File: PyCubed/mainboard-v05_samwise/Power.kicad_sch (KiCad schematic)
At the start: 66 parts, among them J14 Conn_01x06, Q1 IRLML2803, Q2 MBT2222ADW1T1, Q22 NDS8434, Q3 MBT2222ADW1T1, U17 BQ25883RGER, U21 TPS7A4501DCQT, U4 ADM1176-1ARMZ-R7, U5 TPS54226PWPRPWP14_2P31X2P46-L, U6 LT3652HVIMSE#PBF

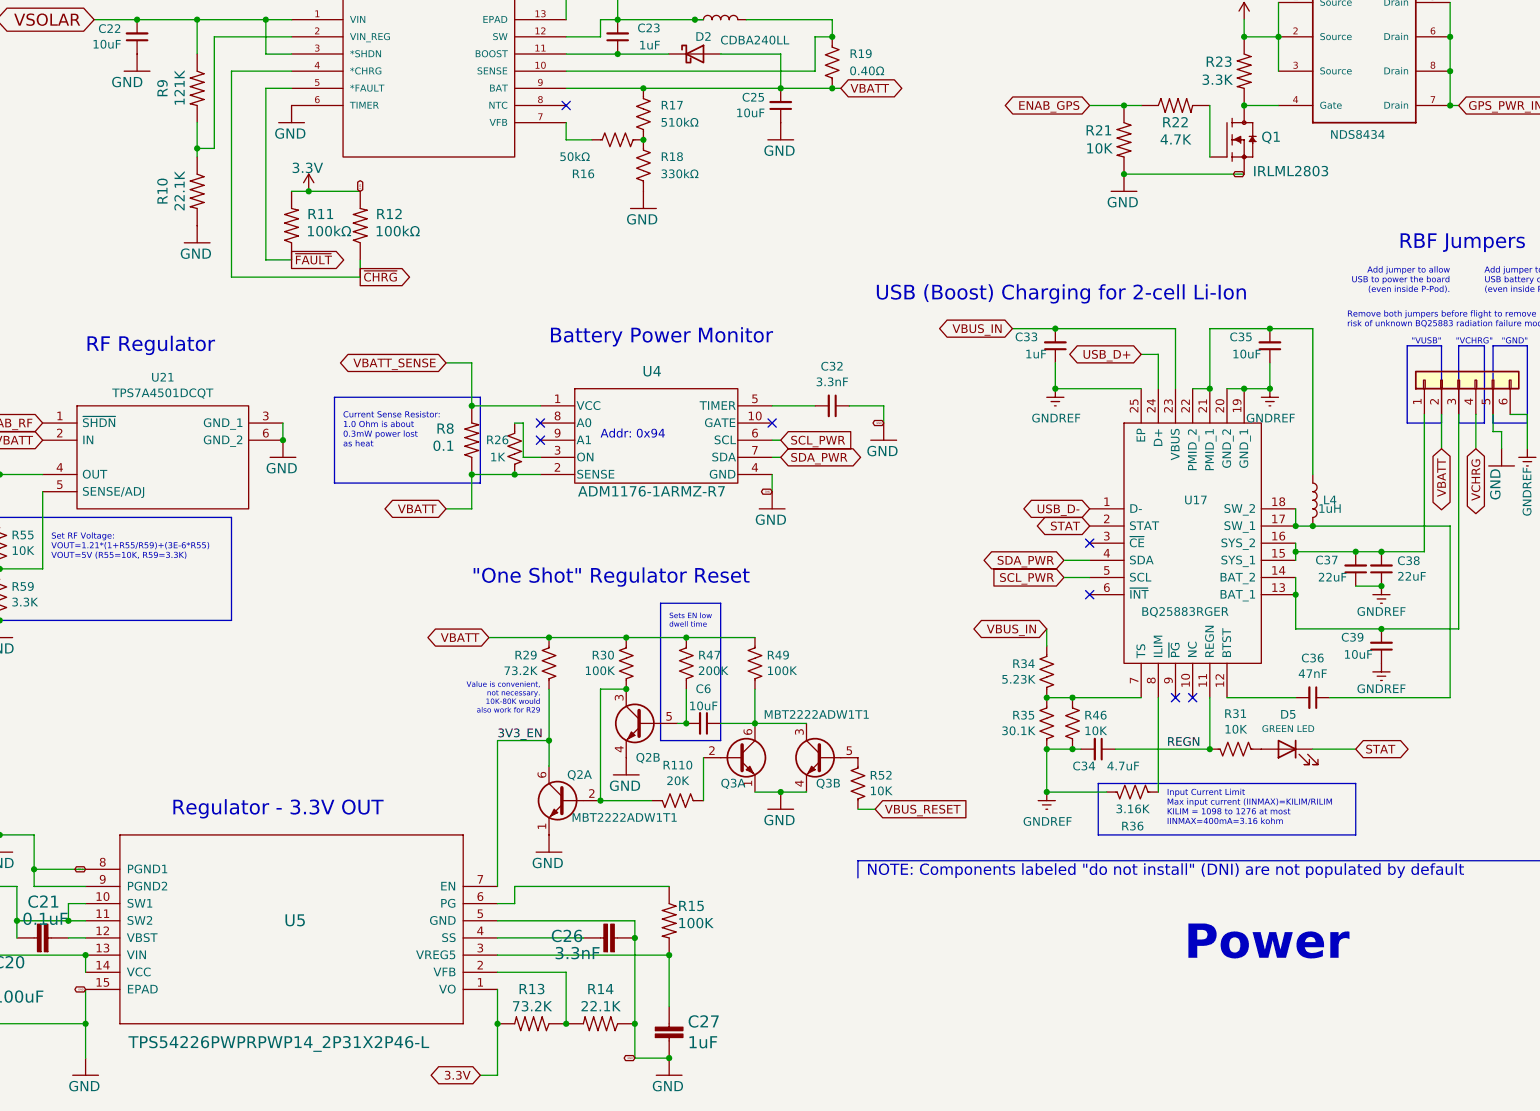
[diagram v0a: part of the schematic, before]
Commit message: added 3D models to Pycubed
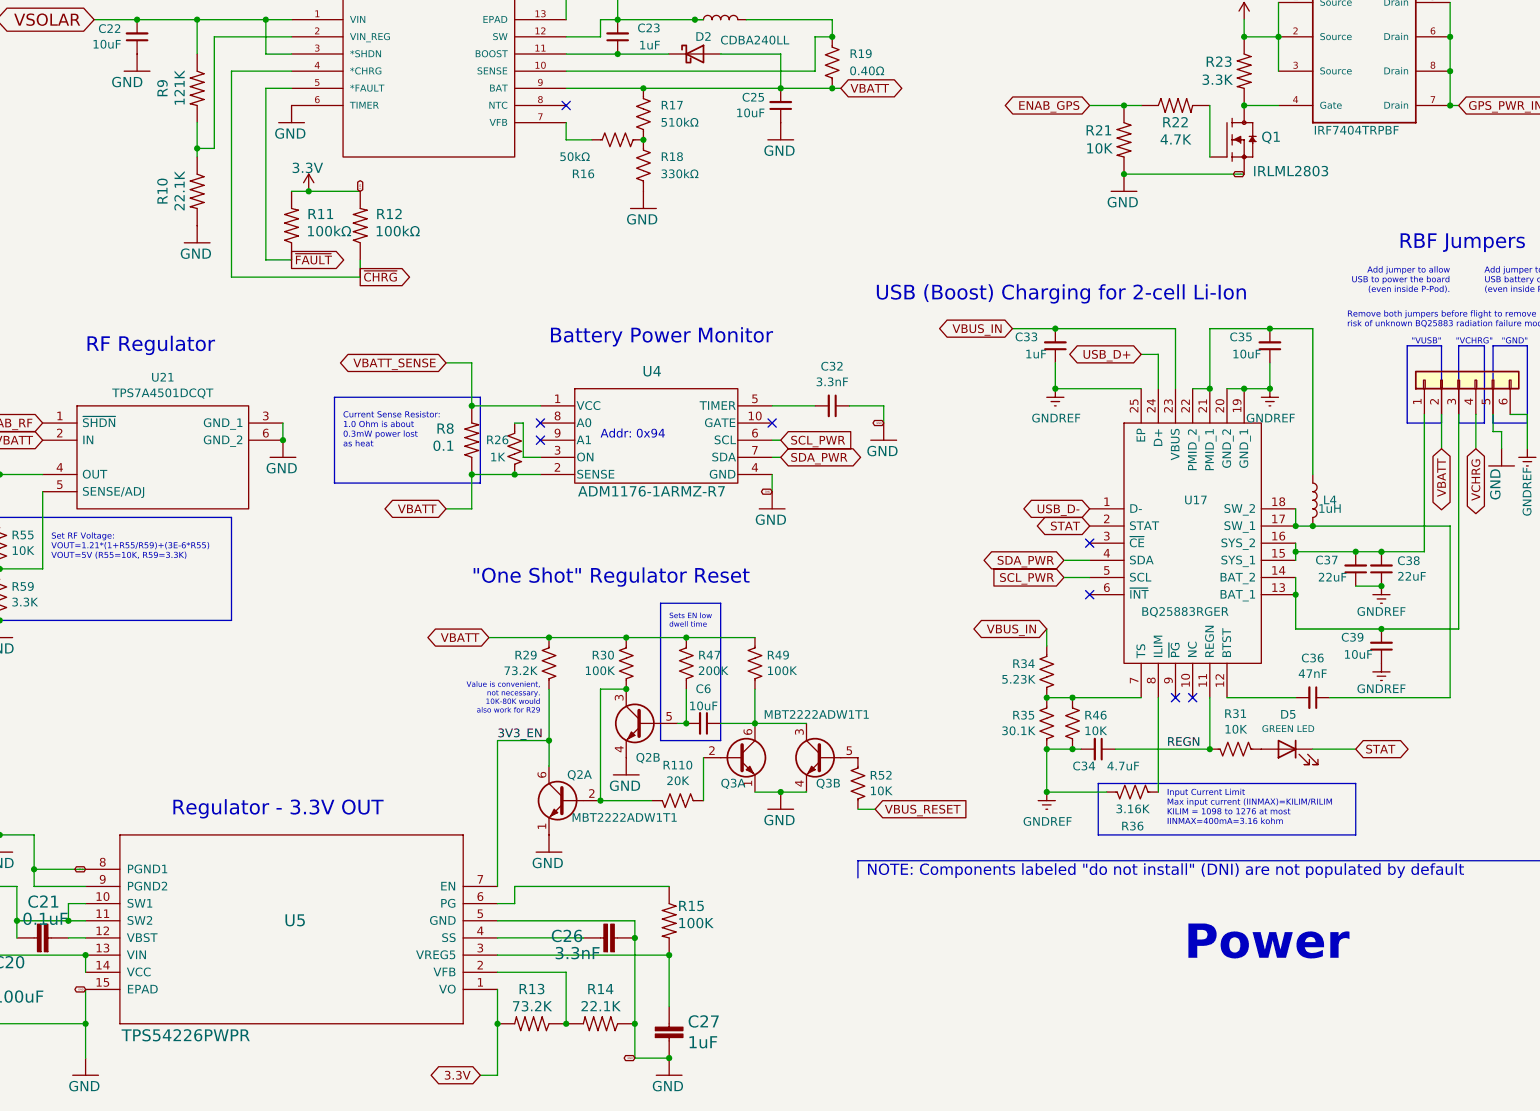
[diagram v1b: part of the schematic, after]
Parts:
- J14: footprint Connector_PinHeader_2.54mm:PinHeader_1x06_P2.54mm_Vertical -> mainboard_local:PinHeader_1x06_P2.54mm_Vertical_J14
- JP6: footprint mainboard:SolderJumper-3_P1.3mm_Bridged12_RoundedPad1.0x1.5mm -> mainboard_local:SolderJumper-3_P1.3mm_Bridged12_RoundedPad1.0x1.5mm_JP6
- Q22: value NDS8434 -> IRF7404TRPBF; footprint mainboard:NDS8434 -> mainboard:IRF7404TRPBF; symbol mainboard:NDS8434 -> mainboard:IRF7404TRPBF; Field7 NDS8434 -> IRF7404TRPBF
- U5: value TPS54226PWPRPWP14_2P31X2P46-L -> TPS54226PWPR
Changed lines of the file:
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@@
     )
   )
-  (symbol (lib_id "mainboard:NDS8434") (at 251.46 43.18 0) (unit 1)
+  (symbol (lib_id "mainboard:IRF7404TRPBF") (at 251.46 43.18 0) (unit 1)
     (in_bom yes) (on_board yes) (dnp no)
     (property "Reference" "Q22" (at 250.19 31.75 0)
       (effects (font (size 1.27 1.27)) (justify left bottom))
     )
-    (property "Value" "NDS8434" (at 246.38 55.88 0)
+    (property "Value" "IRF7404TRPBF" (at 243.967 55.245 0)
       (effects (font (size 1.27 1.27)) (justify left bottom))
     )
-    (property "Footprint" "mainboard:NDS8434" (at 251.46 43.18 0)
+    (property "Footprint" "mainboard:IRF7404TRPBF" (at 251.46 43.18 0)
       (effects (font (size 1.27 1.27)) (justify left bottom) hide)
     )
-    (property "Datasheet" "https://www.onsemi.com/pdf/datasheet/nds8434-d.pdf" (at 251.46 43.18 0)
+    (property "Datasheet" "https://www.infineon.com/dgdl/irf7404pbf.pdf?fileId=5546d462533600a4015355fa31be1ba0" (at 251.46 43.18 0)
       (effects (font (size 1.27 1.27)) (justify left bottom) hide)
     )
@@
       (effects (font (size 1.27 1.27)) (justify left bottom) hide)
     )
-    (property "Field7" "NDS8434" (at 251.46 43.18 0)
+    (property "Field7" "IRF7404TRPBF" (at 251.46 43.18 0)
       (effects (font (size 1.27 1.27)) (justify left bottom) hide)
     )
@@
       (effects (font (size 1.27 1.27)) (justify right) hide)
     )
-    (property "Footprint" "Connector_PinHeader_2.54mm:PinHeader_1x06_P2.54mm_Vertical" (at 265.43 91.44 0)
+    (property "Footprint" "mainboard_local:PinHeader_1x06_P2.54mm_Vertical_J14" (at 265.43 91.44 0)
       (effects (font (size 1.27 1.27)) hide)
     )
@@
       (effects (font (size 1.27 1.27)) (justify left) hide)
     )
-    (property "Footprint" "mainboard:SolderJumper-3_P1.3mm_Bridged12_RoundedPad1.0x1.5mm" (at 30.48 100.33 0)
+    (property "Footprint" "mainboard_local:SolderJumper-3_P1.3mm_Bridged12_RoundedPad1.0x1.5mm_JP6" (at 30.48 100.33 0)
       (effects (font (size 1.27 1.27)) hide)
     )
@@
       (effects (font (size 1.7526 1.7526)) (justify left bottom))
     )
-    (property "Value" "TPS54226PWPRPWP14_2P31X2P46-L" (at 68.58 190.5 0)
+    (property "Value" "TPS54226PWPR" (at 67.564 189.484 0)
       (effects (font (size 1.7526 1.7526)) (justify right top))
     )

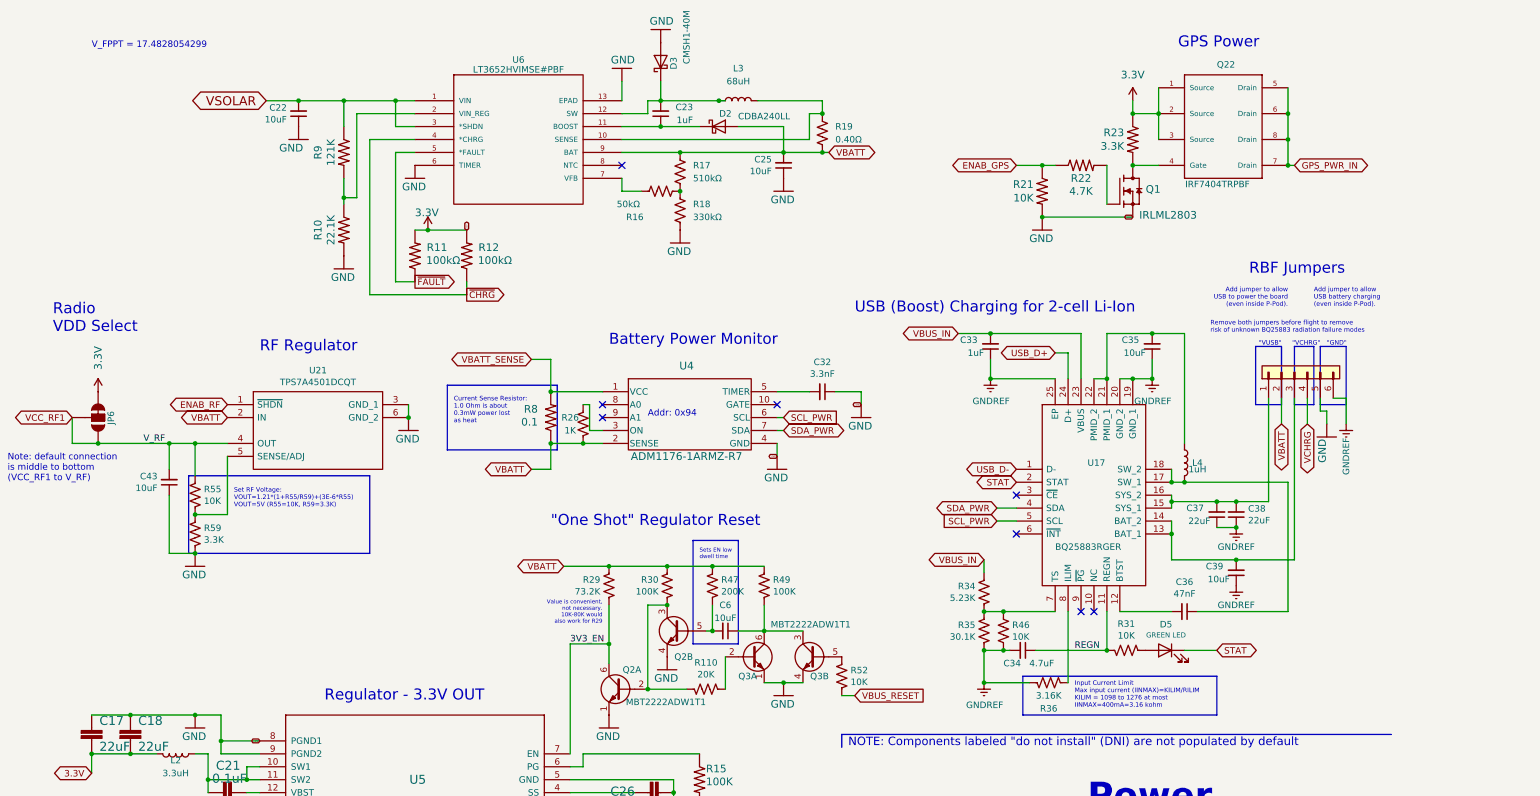
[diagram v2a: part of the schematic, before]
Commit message: Deleted some things, added TODOs to Pycubed
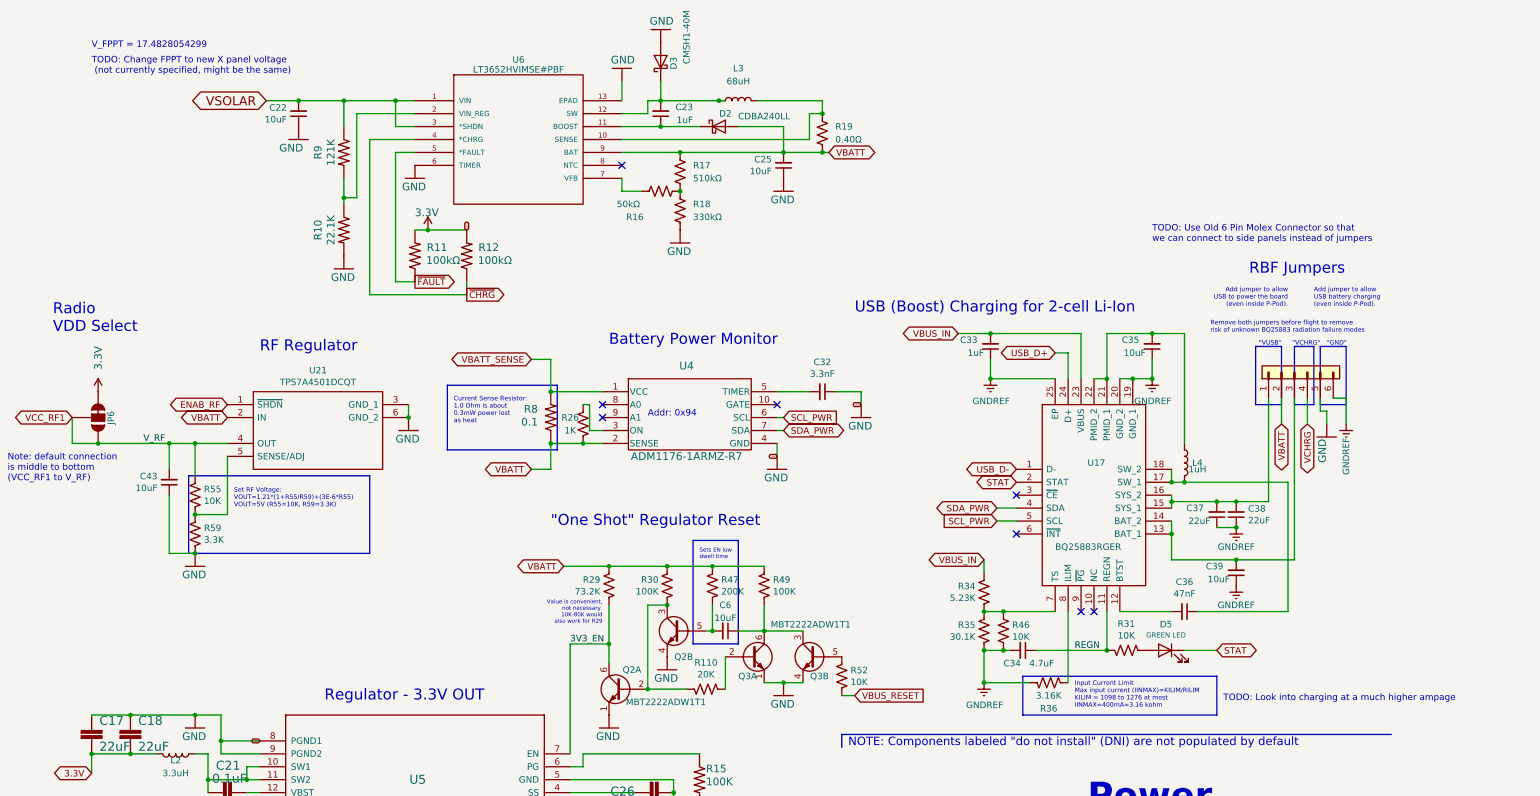
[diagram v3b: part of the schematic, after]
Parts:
- removed Q1: IRLML2803, mainboard:SOT-23, symbol mainboard:IRLML2803TRPBF
- removed Q22: IRF7404TRPBF, mainboard:IRF7404TRPBF, symbol mainboard:IRF7404TRPBF
- removed R21: 10K, Resistor_SMD:R_0603_1608Metric, symbol mainboard:R-US_R0603
- removed R22: 4.7K, Resistor_SMD:R_0603_1608Metric, symbol mainboard:R-US_R0603
- removed R23: 3.3K, Resistor_SMD:R_0603_1608Metric, symbol mainboard:R-US_R0603
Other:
- note added: "TODO: Change FPPT to new X panel voltage (not currently specified, might be the same)"
- note added: "TODO: Look into charging at a much higher ampage"
- note added: "TODO: Use Old 6 Pin Molex Connector so that we can connect to side panels instead of jumpers"
- note removed: "GPS Power"

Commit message: made some changes to mainboard
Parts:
- added J19: Conn_01x06, symbol Connector_Generic:Conn_01x06
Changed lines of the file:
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@@
   )
   (text "Remove both jumpers before flight to remove\nrisk of unknown BQ25883 radiation failure modes\n"
-    (at 248.92 83.82 0)
+    (at 220.98 50.8 0)
     (effects (font (size 0.889 0.889)) (justify left bottom))
   )
@@
   )
   (text "TODO: Use Old 6 Pin Molex Connector so that \nwe can connect to side panels instead of jumpers\n"
-    (at 237.49 66.04 0)
+    (at 353.06 55.88 0)
     (effects (font (size 1.27 1.27) (color 255 0 0 1)) (justify left bottom))
   )
@@
   )
   (text "Add jumper to allow\nUSB to power the board\n(even inside P-Pod).\n"
-    (at 264.16 78.74 0)
+    (at 236.22 45.72 0)
     (effects (font (size 0.889 0.889)) (justify right bottom))
   )
@@
     (effects (font (size 1.651 1.651)) (justify left bottom))
   )
-  (text "RBF Jumpers" (at 256.54 72.39 0)
+  (text "RBF Jumpers" (at 228.6 39.37 0)
     (effects (font (size 2.159 2.159)) (justify left bottom))
   )
   (text "Add jumper to allow\nUSB battery charging\n(even inside P-Pod).\n"
-    (at 269.24 78.74 0)
+    (at 241.3 45.72 0)
     (effects (font (size 0.889 0.889)) (justify left bottom))
   )
@@
         )
       )
+    )
+  )
+  (symbol (lib_id "Connector_Generic:Conn_01x06") (at 264.16 58.42 90) (unit 1)
+    (in_bom yes) (on_board yes) (dnp no) (fields_autoplaced)
+    (property "Reference" "J19" (at 265.43 52.07 90)
+      (effects (font (size 1.27 1.27)))
+    )
+    (property "Value" "Conn_01x06" (at 265.43 54.61 90)
+      (effects (font (size 1.27 1.27)))
+    )
+    (property "Footprint" "" (at 264.16 58.42 0)
+      (effects (font (size 1.27 1.27)) hide)
+    )
+    (property "Datasheet" "~" (at 264.16 58.42 0)
+      (effects (font (size 1.27 1.27)) hide)
+    )
+    (pin "1")
+    (pin "2")
+    (pin "3")
+    (pin "4")
+    (pin "5")
+    (pin "6")
+    (instances
+      (project "mainboard"
+        (path "/db20b18b-d25a-428e-8229-70a189e1de75/00000000-0000-0000-0000-00005cec5dde"
+          (reference "J19") (unit 1)
+        )
+      )
